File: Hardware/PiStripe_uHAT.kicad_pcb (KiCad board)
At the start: 2 copper layers, 65 x 30 mm, 43 parts, among them J1 +12V, J2 LEDs, J3 IRRX, J4 RPi_GPIO, Q1 DMG2305UX-13, Q2 IRF8721PBF-1, Q3 IRF8721PBF-1, Q4 IRF8721PBF-1, U1 TPS54202, U2 DMMT5401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

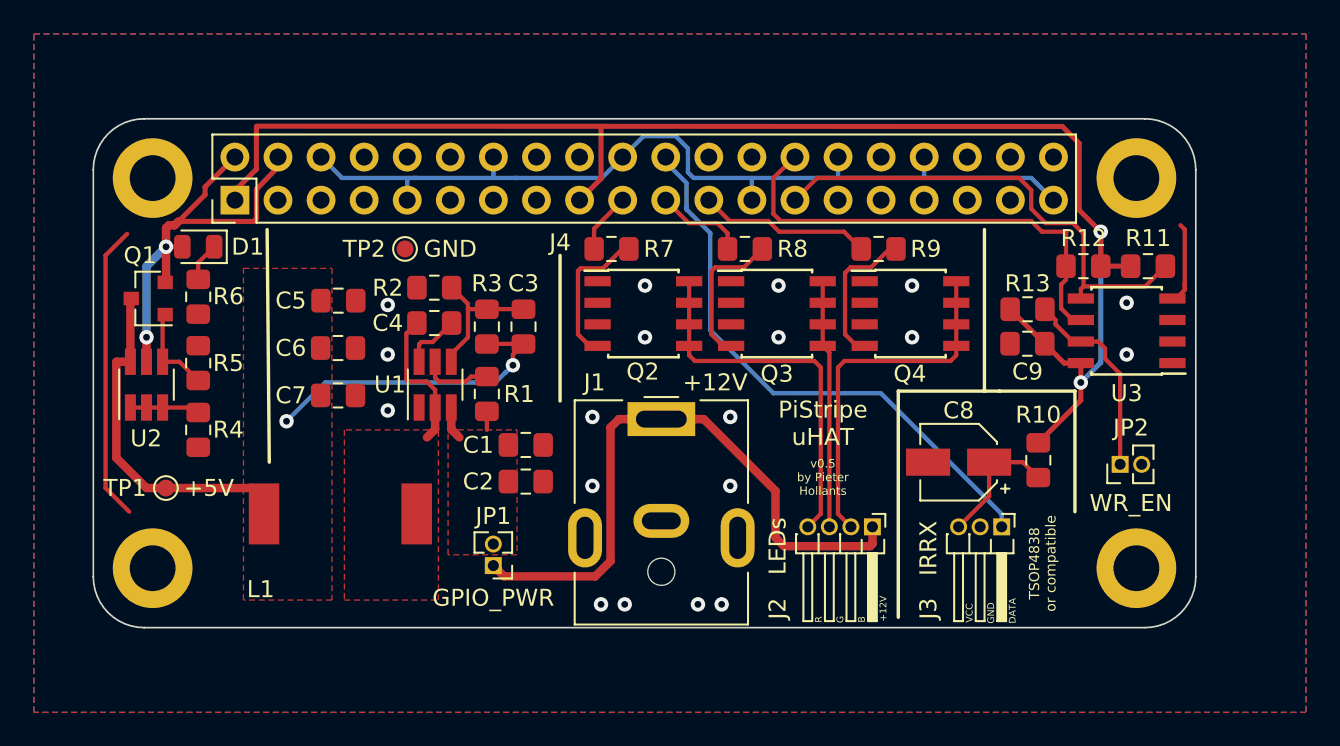
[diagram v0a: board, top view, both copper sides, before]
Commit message: v0.6: Pulldowns for GPIO 09-11, reroute IRRX DATA, correct footprints etc.
- Added pulldown resistors on GPIO 09-11, the gate lines of the IRF8721PBFs
  to ensure an undefined state at powerup doesn't cause the MOSFETs to
  operate and make the LEDs flicker.
- Named nets in schematic for easier tracing in the PCB design.
- Rerouted IRRX DATA line on top side to avoid long GND-dividing trace on
  bottom side.
- Corrected parts and footprints for JP1 and JP2 to 2,54mm instead of
  1,27mm since these are supposed to be opened or closed via jumpers.
- Corrected part and footprint for J4 to a pin socket instead of a pin
  header since the PCB is supposed to be stacked on top of the Raspberry
  Pi. If you want to stack other uHATs on top of the PiStripe HAT, you
  can alternatively use a stacking header such as Adafruit's 1979, the
  pin holes are the same.
- Added more Vias to the ground plane on the bottom side.
- Added text on top side indicating Pin 1 of parts and LED orientation.
- Removed orphaned trace hidden underneath mounting hole 1.

Thanks to @xor@chaos.social and @struppi@chaos.social for their design
review and advice!
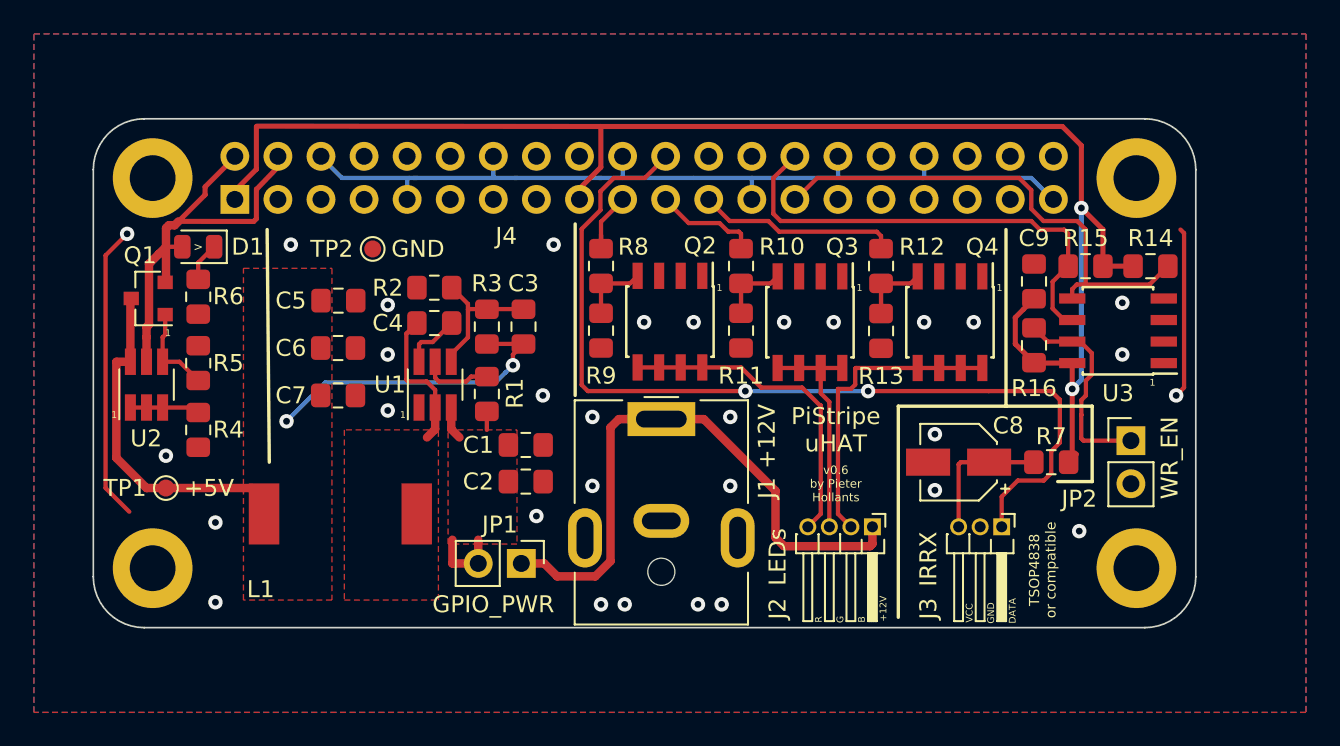
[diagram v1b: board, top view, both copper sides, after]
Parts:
- removed the R10 at (204.2, 95.1)
- added R11: 4K7, Resistor_SMD:R_0805_2012Metric_Pad1.15x1.40mm_HandSolder, F.Cu at (186.7, 87.5)
- added R16: 1K, Resistor_SMD:R_0805_2012Metric_Pad1.15x1.40mm_HandSolder, F.Cu at (204.0, 88.4)
- added R8: 200, Resistor_SMD:R_0805_2012Metric_Pad1.15x1.40mm_HandSolder, F.Cu at (178.4, 83.7)
- added R9: 4K7, Resistor_SMD:R_0805_2012Metric_Pad1.15x1.40mm_HandSolder, F.Cu at (178.4, 87.5)
- C1, C2: value 10uF/50V -> 10uF/25V
- C4: value 100nF/50V -> 100nF/25V
- D1: value LED -> Red
- J4: footprint Connector_PinHeader_2.54mm:PinHeader_2x20_P2.54mm_Vertical -> Connector_PinSocket_2.54mm:PinSocket_2x20_P2.54mm_Vertical; moved to B.Cu
- JP1, JP2: footprint Connector_PinHeader_1.27mm:PinHeader_1x02_P1.27mm_Vertical -> Connector_PinHeader_2.54mm:PinHeader_1x02_P2.54mm_Vertical
- R13: value 1K -> 4K7
- R14: renamed from R11; value 4.7K -> 4K7
- R15: renamed from R12; value 4.7K -> 4K7
- R2: value 13.7K -> 13K7
- R7: value 200 -> 470
- moved R7 28.8 mm to (205.0, 95.2)
- moved R13 8.73 mm to (194.9, 87.5), turned to 270 degrees
- moved C9 3.69 mm to (204.0, 84.6), turned to 270 degrees
- moved Q4 2.38 mm to (199.0, 87.0), turned to 270 degrees
- moved Q3 2.01 mm to (190.8, 87.0), turned to 270 degrees
- moved TP2 1.90 mm to (165.0, 82.7)
- moved JP1 1.66 mm to (173.7, 101.2), turned to 270 degrees
- moved Q2 1.64 mm to (182.5, 87.0), turned to 270 degrees
- moved JP2 1.53 mm to (209.7, 94.0), turned to 0 degrees
- moved R10 1.03 mm to (186.7, 83.7), turned to 270 degrees
- moved R12 1.02 mm to (194.9, 83.7), turned to 270 degrees
- moved U3 0.51 mm to (208.9, 87.5)
- moved R14 0.15 mm to (210.8, 83.7)
- moved R15 0.13 mm to (207.0, 83.7)
- turned J4 to 270 degrees
- renumbered R8 to R10, R9 to R12
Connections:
- net Net-(C1-Pad1) renamed /TPS_12V
- net Net-(C3-Pad1) renamed /TPS_FB
- net Net-(C3-Pad2) renamed /TPS_5V
- net Net-(C4-Pad1) renamed /TPS_BOOT
- net Net-(C4-Pad2) renamed /TPS_SW
- net Net-(D1-Pad2) renamed /+5V
- net Net-(J2-Pad2) renamed /B_DRAIN
- net Net-(J2-Pad3) renamed /G_DRAIN
- net Net-(J2-Pad4) renamed /R_DRAIN
- net Net-(J3-Pad1) renamed /IRRX_DATA
- net Net-(J4-Pad21) renamed /GPIO09
- net Net-(J4-Pad23) renamed /GPIO11
- net Net-(J4-Pad27) renamed /ID_SDA
- net Net-(J4-Pad28) renamed /ID_SCL
- net Net-(Q3-Pad4) renamed /G_GATE
- net Net-(R1-Pad2) renamed /TPS_EN
- C8 pad 1: Net-(C8-Pad1) -> /IRRX_3V3
- J3 pad 3: Net-(C8-Pad1) -> /IRRX_3V3
- J4 pad 19: Net-(J4-Pad19) -> /GPIO10
- JP2 pad 1: Net-(JP2-Pad1) -> /ID_WP
- Q2 pad 4: Net-(Q2-Pad4) -> /R_GATE
- Q4 pad 4: Net-(Q4-Pad4) -> /B_GATE
- R12 pad 2: Net-(Q4-Pad4) -> /B_GATE
- R13 pad 1: +3V3 -> /B_GATE
- R13 pad 2: Net-(JP2-Pad1) -> GND
- R7 pad 1: Net-(J4-Pad19) -> /IRRX_3V3
- R7 pad 2: Net-(Q2-Pad4) -> +3V3
- U3 pad 7: Net-(JP2-Pad1) -> /ID_WP
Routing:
- net /IRRX_DATA: track 33.9 -> 55.2 mm, vias 0 -> 2
- net /ID_WP: track 0.00 -> 13.4 mm
- net Net-(JP2-Pad1): track 11.9 -> 0.00 mm
- net Net-(Q2-Pad4): track 8.71 -> 0.00 mm
- net Net-(Q4-Pad4): track 8.65 -> 0.00 mm
- net Net-(C8-Pad1): track 8.33 -> 0.00 mm
- net /IRRX_3V3: track 0.00 -> 8.17 mm
- net /G_GATE: track 8.71 -> 4.08 mm
- net /TPS_12V: track 3.05 -> 7.37 mm
- net GND: track 77.3 -> 81.6 mm, vias 19 -> 31
- net /GPIO10: track 0.00 -> 4.21 mm
- net /B_GATE: track 0.00 -> 4.11 mm
- net /R_GATE: track 0.00 -> 4.10 mm
- net +3V3: track 90.1 -> 94.0 mm
- net Net-(J4-Pad19): track 3.57 -> 0.00 mm
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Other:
- outline, holes or cut-outs redrawn
- board text added: "1"
- board text added: ">"
- board text added: "v0.6 by Pieter Hollants"
- board text removed: "v0.5 by Pieter Hollants"

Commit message: v0.7: Correct connections and footprints for J2 and J3
- Corrected J2 connections from R/G/B/+12V to B/R/G/+12V layout
  because that's what most LED strips actually use connector-wise.
- Flipped J3 connections, Pin 1/DATA is now left, so that you can
  solder in a TSOP4838 directly if you want to.
- Corrected footprints for J2 and J3 to 2.54mm pitch.
- This required moving J1 and the entire voltage regulator
  section a bit to the left, rotating U3 and rearranging related
  parts as well as moving R7 and C8 for the TSOP.
- Changed JP2 to 1.27mm pitch again because there are actually
  1.27mm jumpers available, the space was needed and this jumper is
  less likely to be changed than JP1.
- Refer to CSV parts list instead of repeating its contents in README
  that easily gets outdated.
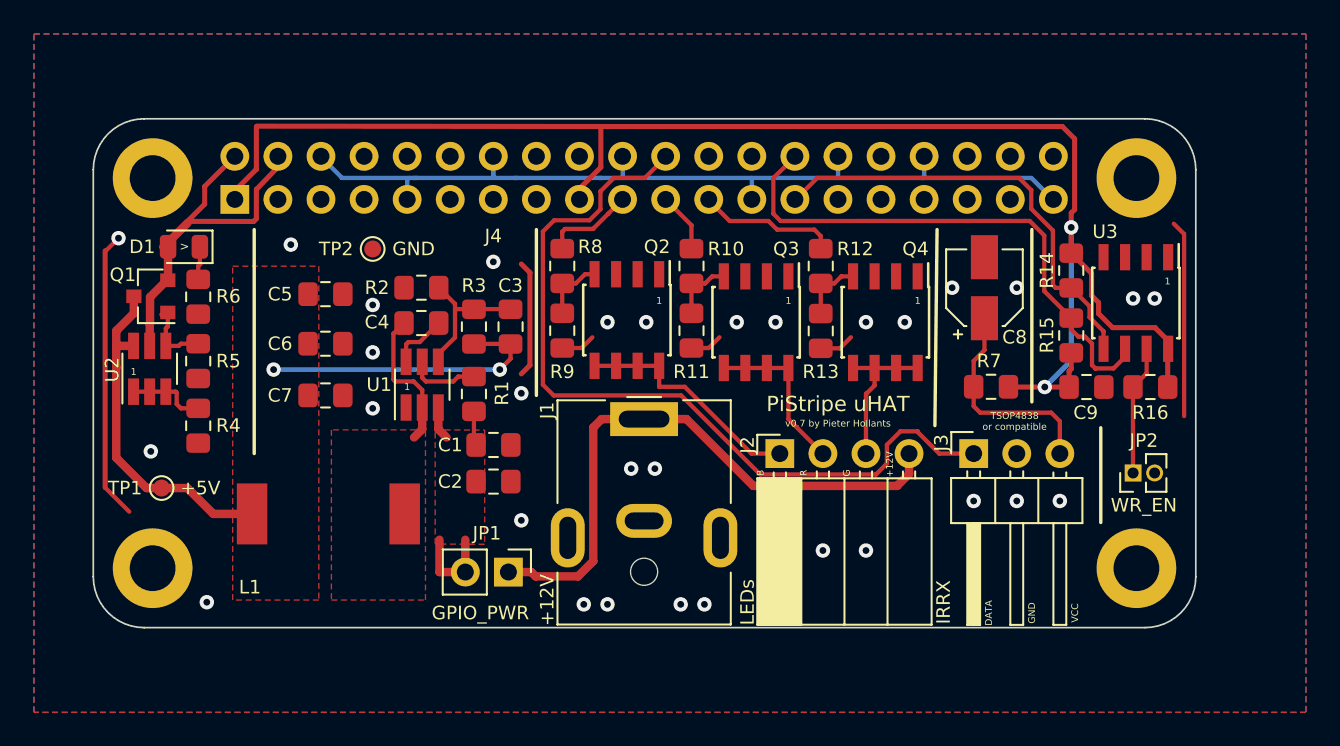
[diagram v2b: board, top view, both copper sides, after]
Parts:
- C9: value 100nF -> 100nF/25V
- J2: footprint Connector_PinHeader_1.27mm:PinHeader_1x04_P1.27mm_Horizontal -> Connector_PinSocket_2.54mm:PinSocket_1x04_P2.54mm_Horizontal
- J3: footprint Connector_PinHeader_1.27mm:PinHeader_1x03_P1.27mm_Horizontal -> pief:PinHeader_1x03_P2.54mm_Horizontal_Mirrored
- JP2: footprint Connector_PinHeader_2.54mm:PinHeader_1x02_P2.54mm_Vertical -> Connector_PinHeader_1.27mm:PinHeader_1x02_P1.27mm_Vertical
- R10, R12, R8: value 200 -> 220
- moved C8 10.4 mm to (201.0, 85.0), turned to 90 degrees
- moved R16 7.29 mm to (210.8, 90.8), turned to 180 degrees
- moved J2 6.96 mm to (189.0, 94.7), turned to 90 degrees
- moved C9 6.95 mm to (207.1, 90.8), turned to 180 degrees
- moved R7 5.69 mm to (201.4, 90.8)
- moved J3 5.51 mm to (205.5, 94.7)
- moved R14 4.68 mm to (206.2, 84.0), turned to 90 degrees
- moved R15 4.17 mm to (206.2, 87.8), turned to 270 degrees
- moved Q4 3.81 mm to (195.2, 87.0)
- moved R12 3.56 mm to (191.4, 83.7)
- moved R13 3.56 mm to (191.4, 87.5)
- moved Q3 3.17 mm to (187.6, 87.0)
- moved R10 2.92 mm to (183.8, 83.7)
- moved R11 2.92 mm to (183.8, 87.5)
- moved Q2 2.54 mm to (180.0, 86.9)
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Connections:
- net Net-(D1-Pad1) renamed /LED_+5V
- net Net-(Q1-Pad1) renamed /DMMT_BC34
- net Net-(R4-Pad2) renamed /DMMT_BC12
- J2 pad 1: +12V -> /B_DRAIN
- J2 pad 2: /B_DRAIN -> /R_DRAIN
- J2 pad 4: /R_DRAIN -> +12V
- Q2 pad 4: /R_GATE -> /B_GATE
- Q2 pad 5: /R_DRAIN -> /B_DRAIN
- Q2 pad 6: /R_DRAIN -> /B_DRAIN
- Q2 pad 7: /R_DRAIN -> /B_DRAIN
- Q2 pad 8: /R_DRAIN -> /B_DRAIN
- Q3 pad 4: /G_GATE -> /R_GATE
- Q3 pad 5: /G_DRAIN -> /R_DRAIN
- Q3 pad 6: /G_DRAIN -> /R_DRAIN
- Q3 pad 7: /G_DRAIN -> /R_DRAIN
- Q3 pad 8: /G_DRAIN -> /R_DRAIN
- Q4 pad 4: /B_GATE -> /G_GATE
- Q4 pad 5: /B_DRAIN -> /G_DRAIN
- Q4 pad 6: /B_DRAIN -> /G_DRAIN
- Q4 pad 7: /B_DRAIN -> /G_DRAIN
- Q4 pad 8: /B_DRAIN -> /G_DRAIN
- R10 pad 2: /G_GATE -> /R_GATE
- R11 pad 1: /G_GATE -> /R_GATE
- R12 pad 2: /B_GATE -> /G_GATE
- R13 pad 1: /B_GATE -> /G_GATE
- R8 pad 2: /R_GATE -> /B_GATE
- R9 pad 1: /R_GATE -> /B_GATE
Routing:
- net GND: track 81.6 -> 96.1 mm
- net /R_DRAIN: track 19.2 -> 10.1 mm
- net /IRRX_DATA: track 55.2 -> 48.9 mm, vias 2 -> 0
- net /+5V: track 27.0 -> 21.6 mm
- net /IRRX_3V3: track 8.17 -> 13.0 mm
- net /G_DRAIN: track 13.4 -> 9.08 mm
- net /ID_SCL: track 28.5 -> 32.7 mm
- net /B_DRAIN: track 18.0 -> 13.8 mm
- net /ID_WP: track 13.4 -> 9.21 mm
- net /GPIO11: track 12.0 -> 8.49 mm
- net /ID_SDA: track 30.0 -> 26.9 mm
- net /GPIO09: track 6.13 -> 3.53 mm
- net /TPS_12V: track 7.37 -> 9.33 mm
- net /DMMT_BC34: track 5.86 -> 4.66 mm
- net /GPIO10: track 4.21 -> 5.34 mm
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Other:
- board text added: "v0.7 by Pieter Hollants"
- board text removed: "v0.6 by Pieter Hollants"
